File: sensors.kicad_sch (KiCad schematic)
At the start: 25 parts, among them J11 GND, J14 3.3v, J15 SDA, J16 SCL, U10 BHI360, U21 PCA9517DP,118, U33 BME688_C3664478, U34 BMI270

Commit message: Remove Badge.Team branding
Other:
- company: Badge.Team -> Nicolai Electronics
- title: WHY2025 badge -> Tanmatsu
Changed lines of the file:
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@@
 	(paper "A4")
 	(title_block
-		(title "WHY2025 badge")
-		(date "2024-11-01")
-		(rev "Prototype 3")
-		(company "Badge.Team")
-		(comment 1 "Copyright 2024 Nicolai Electronics")
-		(comment 2 "License: CERN-OHL-P")
-		(comment 3 "Untested prototype design")
+		(title "Tanmatsu")
+		(date "2024-11-20")
+		(rev "Prototype 4")
+		(company "Nicolai Electronics")
+		(comment 1 "Copyright 2024 Paul Honig")
+		(comment 2 "Copyright 2024 Nicolai Electronics")
+		(comment 3 "License: CERN-OHL-P")
 	)
 	(junction

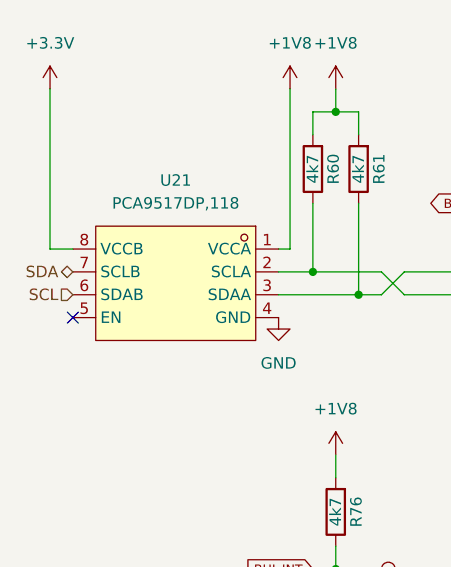
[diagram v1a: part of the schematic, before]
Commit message: Fix SDA/SCL swap.
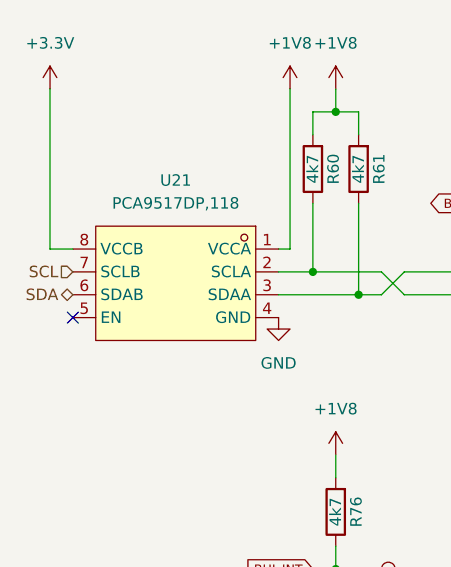
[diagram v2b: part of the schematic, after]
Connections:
- net SCL: now also U21.7 (SCLB); no longer U21.6 (SDAB)
- net SDA: now also U21.6 (SDAB); no longer U21.7 (SCLB)
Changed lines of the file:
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@@
 	(hierarchical_label "SCL"
 		(shape input)
-		(at 33.02 63.5 180)
+		(at 33.02 60.96 180)
 		(fields_autoplaced yes)
 		(effects
@@
 	(hierarchical_label "SDA"
 		(shape bidirectional)
-		(at 33.02 60.96 180)
+		(at 33.02 63.5 180)
 		(fields_autoplaced yes)
 		(effects

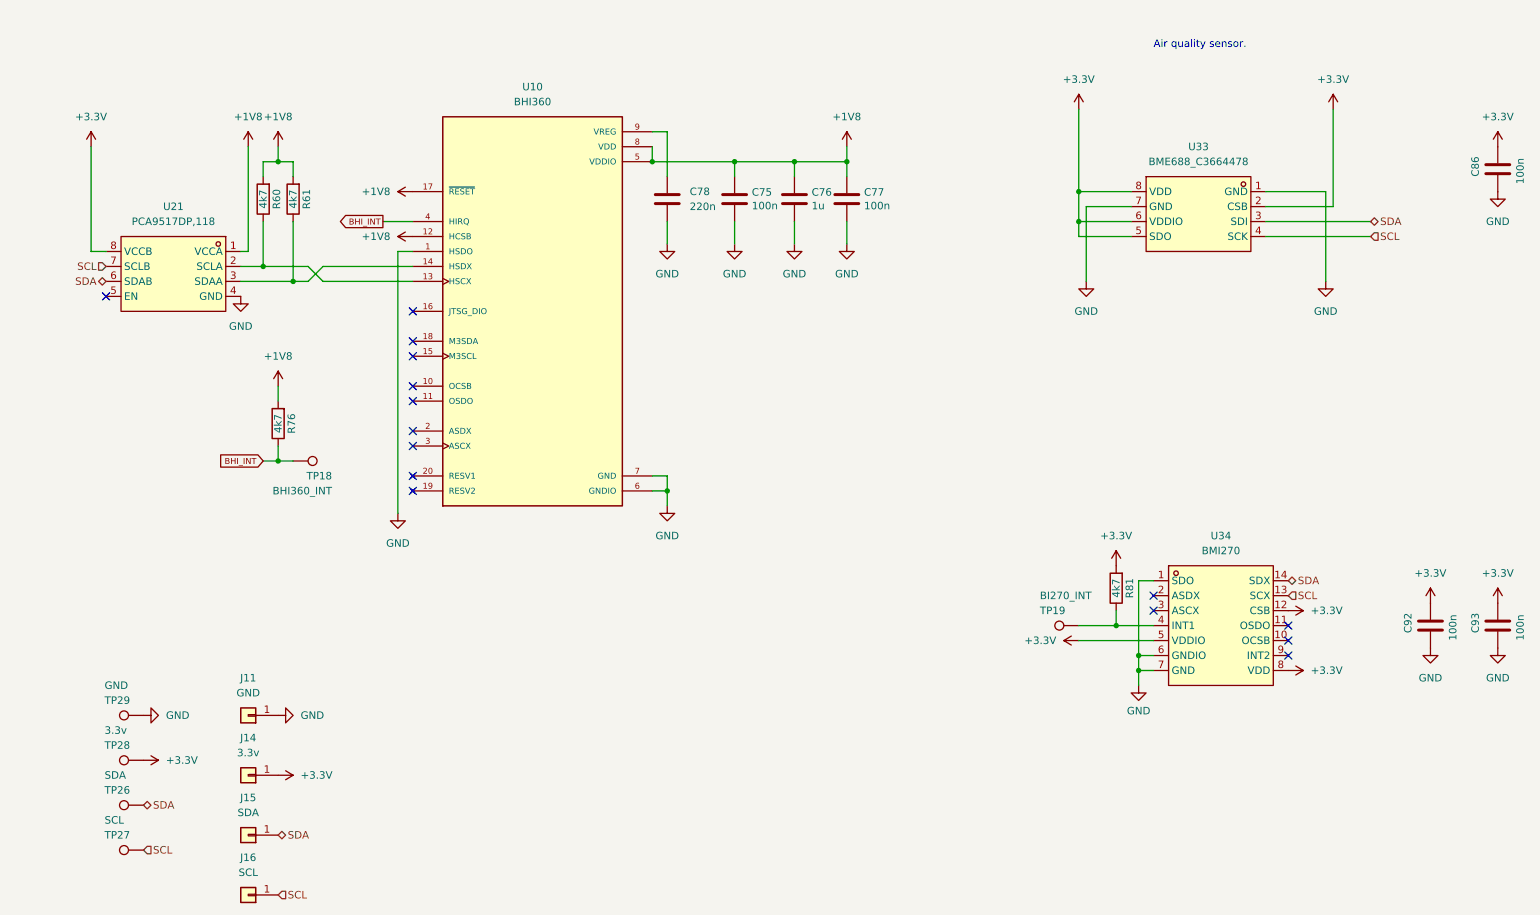
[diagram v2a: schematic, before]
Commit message: Remove Bosch sensors, add header for CO2 sensor
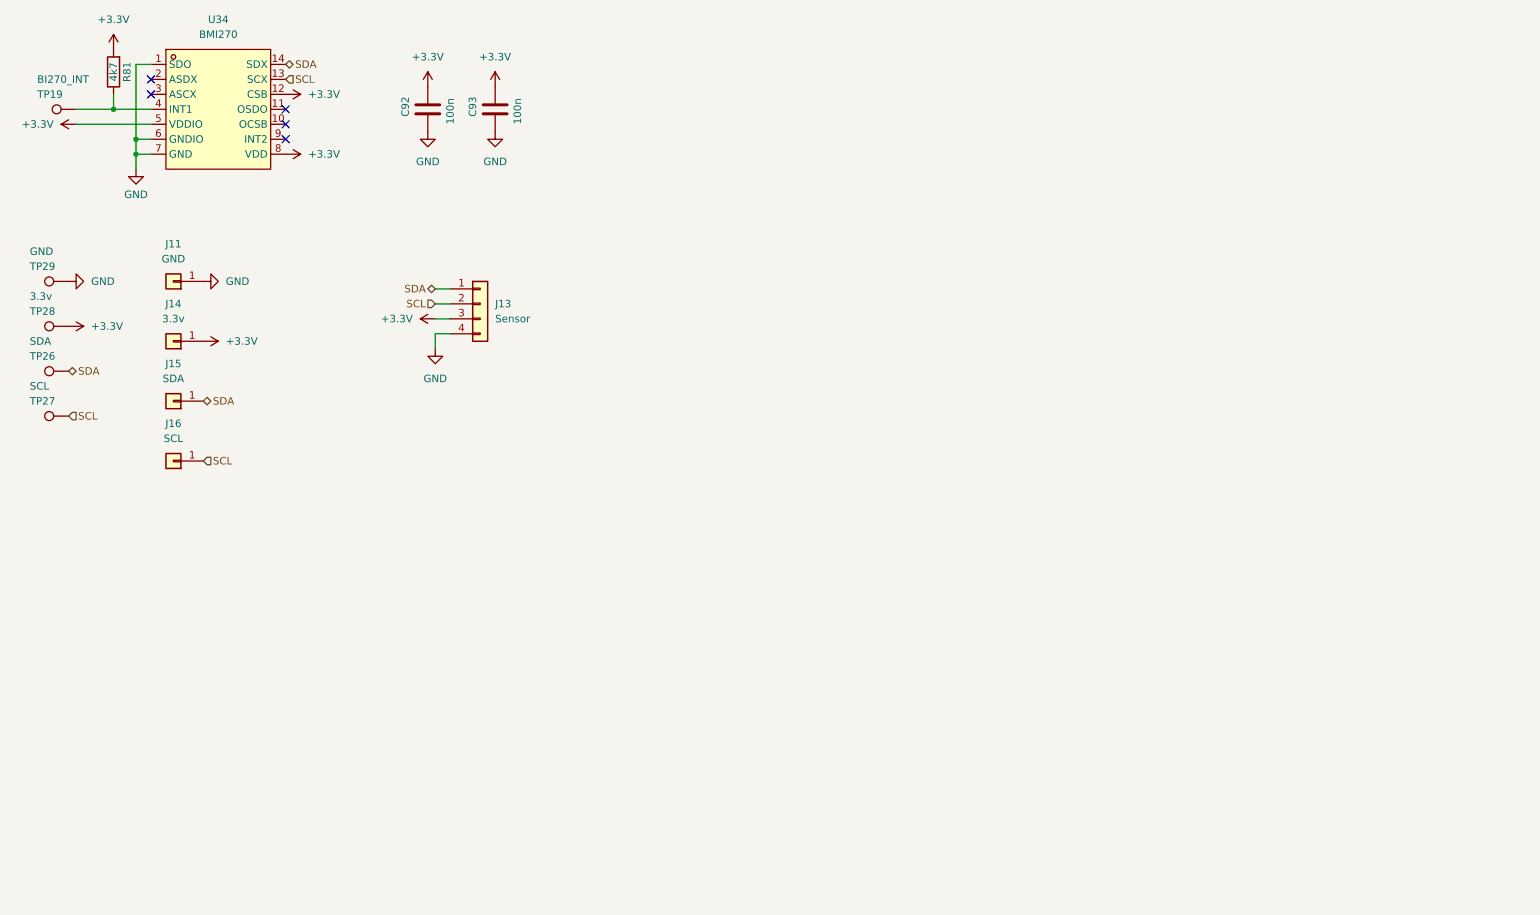
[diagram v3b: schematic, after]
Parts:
- removed C75, C77: 100n, Capacitor_SMD:C_0402_1005Metric, symbol symbols:C
- removed C76: 1u, Capacitor_SMD:C_0603_1608Metric, symbol symbols:C
- removed C78: 220n, Capacitor_SMD:C_0603_1608Metric, symbol Device:C
- removed C86: 100n, Capacitor_SMD:C_0402_1005Metric, symbol mch2021-rescue:C-Device
- removed R60, R61, R76: 4k7, Resistor_SMD:R_0402_1005Metric, symbol Device:R
- removed TP18: BHI360_INT, TestPoint:TestPoint_Pad_D1.0mm, symbol Connector:TestPoint
- removed U10: BHI360, library:XDCR_BHI360, symbol BHI360:BHI360
- removed U21: PCA9517DP,118, library:TSSOP-8_L3.0-W3.0-P0.65-LS4.9-BL, symbol lcsc:PCA9517DP,118
- removed U33: BME688_C3664478, lcsc:LGA-8_L3.0-W3.0-P0.80_BME688, symbol lcsc:BME688_C3664478
- added J13: Sensor, Connector_PinHeader_2.54mm:PinHeader_1x04_P2.54mm_Vertical, symbol Connector_Generic:Conn_01x04
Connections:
- net +3.3V: now also J13.3 (Pin_3)
- net GND: now also J13.4 (Pin_4)
- net SCL: now also J13.2 (Pin_2)
- net SDA: now also J13.1 (Pin_1)
- no-connect marks 15 -> 5
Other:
- note removed: "Air quality sensor."
- moved on the sheet: C92, C93, J11, J14, J15, J16, R81, TP19, TP26, TP27, TP28, TP29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

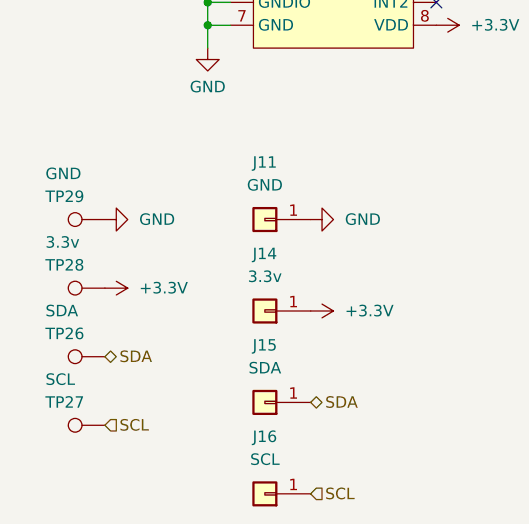
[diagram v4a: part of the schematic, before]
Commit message: Add MCH2022 style battery connector as DNP, use correct footprint for PH style battery connector
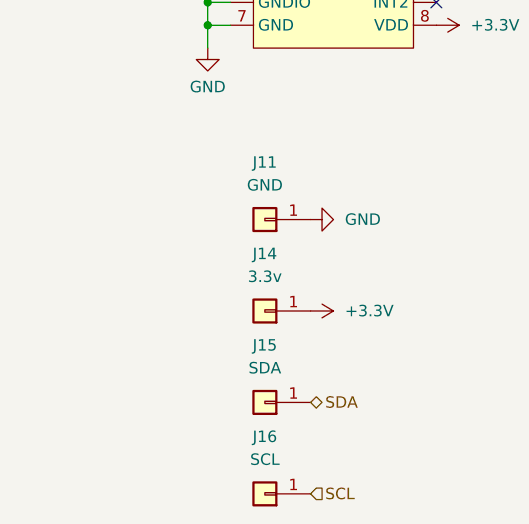
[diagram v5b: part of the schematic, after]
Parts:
- removed TP26: SDA, TestPoint:TestPoint_Pad_D1.0mm, symbol Connector:TestPoint
- removed TP27: SCL, TestPoint:TestPoint_Pad_D1.0mm, symbol Connector:TestPoint
- removed TP28: 3.3v, TestPoint:TestPoint_Pad_D1.0mm, symbol Connector:TestPoint
- removed TP29: GND, TestPoint:TestPoint_Pad_D1.0mm, symbol Connector:TestPoint

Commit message: Tanmatsu prototype
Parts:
- renumbered C92 to C83, C93 to C84, J11 to J15, J13 to J16, J14 to J17, J15 to J18, J16 to J19, R81 to R82, TP19 to TP22, U34 to U30
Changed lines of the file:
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@@
 	(title_block
 		(title "Tanmatsu")
-		(date "2024-12-24")
-		(rev "Prototype")
+		(date "2024-12-30")
+		(rev "0.9")
 		(company "Nicolai Electronics")
 		(comment 1 "Copyright 2024 Paul Honig")
@@
 		(dnp no)
 		(fields_autoplaced yes)
-		(property "Reference" "#PWR0310"
+		(property "Reference" "#PWR0293"
 			(at 45.72 73.66 0)
 			(effects
@@
 			(project "why2025"
 				(path "/6a31734e-65de-48f3-8156-2b24b665b183/14d9c0ee-00ab-4a1b-b059-e8045c71d6ae"
-					(reference "#PWR0310")
+					(reference "#PWR0293")
 					(unit 1)
 				)
@@
 		(on_board yes)
 		(dnp no)
-		(property "Reference" "#PWR0306"
+		(property "Reference" "#PWR0287"
 			(at 87.63 44.45 0)
 			(effects
@@
 			(project "why2025"
 				(path "/6a31734e-65de-48f3-8156-2b24b665b183/14d9c0ee-00ab-4a1b-b059-e8045c71d6ae"
-					(reference "#PWR0306")
+					(reference "#PWR0287")
 					(unit 1)
 				)
@@
 		(dnp no)
 		(fields_autoplaced yes)
-		(property "Reference" "J14"
+		(property "Reference" "J17"
 			(at 44.45 67.31 0)
 			(effects
@@
 			(project "why2025"
 				(path "/6a31734e-65de-48f3-8156-2b24b665b183/14d9c0ee-00ab-4a1b-b059-e8045c71d6ae"
-					(reference "J14")
+					(reference "J17")
 					(unit 1)
 				)
@@
 		(dnp no)
 		(fields_autoplaced yes)
-		(property "Reference" "#PWR0288"
+		(property "Reference" "#PWR0289"
 			(at 59.69 41.91 0)
 			(effects
@@
 			(project "why2025"
 				(path "/6a31734e-65de-48f3-8156-2b24b665b183/14d9c0ee-00ab-4a1b-b059-e8045c71d6ae"
-					(reference "#PWR0288")
+					(reference "#PWR0289")
 					(unit 1)
 				)
@@
 		(dnp no)
 		(fields_autoplaced yes)
-		(property "Reference" "#PWR0304"
+		(property "Reference" "#PWR0285"
 			(at 59.69 31.75 0)
 			(effects
@@
 			(project "why2025"
 				(path "/6a31734e-65de-48f3-8156-2b24b665b183/14d9c0ee-00ab-4a1b-b059-e8045c71d6ae"
-					(reference "#PWR0304")
+					(reference "#PWR0285")
 					(unit 1)
 				)
@@
 		(on_board yes)
 		(dnp no)
-		(property "Reference" "TP19"
+		(property "Reference" "TP22"
 			(at 21.336 31.75 90)
 			(effects
@@
 			(project "why2025"
 				(path "/6a31734e-65de-48f3-8156-2b24b665b183/14d9c0ee-00ab-4a1b-b059-e8045c71d6ae"
-					(reference "TP19")
+					(reference "TP22")
 					(unit 1)
 				)
@@
 		(dnp no)
 		(fields_autoplaced yes)
-		(property "Reference" "J11"
+		(property "Reference" "J15"
 			(at 44.45 57.15 0)
 			(effects
@@
 			(project "why2025"
 				(path "/6a31734e-65de-48f3-8156-2b24b665b183/14d9c0ee-00ab-4a1b-b059-e8045c71d6ae"
-					(reference "J11")
+					(reference "J15")
 					(unit 1)
 				)
@@
 		(dnp no)
 		(fields_autoplaced yes)
-		(property "Reference" "#PWR0309"
+		(property "Reference" "#PWR0291"
 			(at 55.88 63.5 0)
 			(effects
@@
 			(project "why2025"
 				(path "/6a31734e-65de-48f3-8156-2b24b665b183/14d9c0ee-00ab-4a1b-b059-e8045c71d6ae"
-					(reference "#PWR0309")
+					(reference "#PWR0291")
 					(unit 1)
 				)
@@
 		(on_board yes)
 		(dnp no)
-		(property "Reference" "C92"
+		(property "Reference" "C83"
 			(at 83.82 35.56 90)
 			(effects
@@
 			(project "why2025"
 				(path "/6a31734e-65de-48f3-8156-2b24b665b183/14d9c0ee-00ab-4a1b-b059-e8045c71d6ae"
-					(reference "C92")
+					(reference "C83")
 					(unit 1)
 				)
@@
 		(dnp no)
 		(fields_autoplaced yes)
-		(property "Reference" "#PWR0305"
+		(property "Reference" "#PWR0283"
 			(at 87.63 34.29 0)
 			(effects
@@
 			(project "why2025"
 				(path "/6a31734e-65de-48f3-8156-2b24b665b183/14d9c0ee-00ab-4a1b-b059-e8045c71d6ae"
-					(reference "#PWR0305")
+					(reference "#PWR0283")
 					(unit 1)
 				)
@@
 		(dnp no)
 		(fields_autoplaced yes)
-		(property "Reference" "J13"
+		(property "Reference" "J16"
 			(at 99.06 67.3099 0)
 			(effects
@@
 			(project ""
 				(path "/6a31734e-65de-48f3-8156-2b24b665b183/14d9c0ee-00ab-4a1b-b059-e8045c71d6ae"
-					(reference "J13")
+					(reference "J16")
 					(unit 1)
 				)
@@
 		(dnp no)
 		(fields_autoplaced yes)
-		(property "Reference" "#PWR0307"
+		(property "Reference" "#PWR0284"
 			(at 99.06 34.29 0)
 			(effects
@@
 			(project "why2025"
 				(path "/6a31734e-65de-48f3-8156-2b24b665b183/14d9c0ee-00ab-4a1b-b059-e8045c71d6ae"
-					(reference "#PWR0307")
+					(reference "#PWR0284")
 					(unit 1)
 				)
@@
 		(dnp no)
 		(fields_autoplaced yes)
-		(property "Reference" "#PWR0115"
+		(property "Reference" "#PWR0292"
 			(at 92.71 69.85 0)
 			(effects
@@
 			(project "tanmatsu"
 				(path "/6a31734e-65de-48f3-8156-2b24b665b183/14d9c0ee-00ab-4a1b-b059-e8045c71d6ae"
-					(reference "#PWR0115")
+					(reference "#PWR0292")
 					(unit 1)
 				)
@@
 		(on_board yes)
 		(dnp no)
-		(property "Reference" "#PWR0279"
+		(property "Reference" "#PWR0290"
 			(at 38.1 50.8 0)
 			(effects
@@
 			(project "why2025"
 				(path "/6a31734e-65de-48f3-8156-2b24b665b183/14d9c0ee-00ab-4a1b-b059-e8045c71d6ae"
-					(reference "#PWR0279")
+					(reference "#PWR0290")
 					(unit 1)
 				)
@@
 		(dnp no)
 		(fields_autoplaced yes)
-		(property "Reference" "J16"
+		(property "Reference" "J19"
 			(at 44.45 87.63 0)
 			(effects
@@
 			(project "why2025"
 				(path "/6a31734e-65de-48f3-8156-2b24b665b183/14d9c0ee-00ab-4a1b-b059-e8045c71d6ae"
-					(reference "J16")
+					(reference "J19")
 					(unit 1)
 				)
@@
 		(dnp no)
 		(fields_autoplaced yes)
-		(property "Reference" "#PWR0280"
+		(property "Reference" "#PWR0286"
 			(at 31.75 36.83 0)
 			(effects
@@
 			(project "why2025"
 				(path "/6a31734e-65de-48f3-8156-2b24b665b183/14d9c0ee-00ab-4a1b-b059-e8045c71d6ae"
-					(reference "#PWR0280")
+					(reference "#PWR0286")
 					(unit 1)
 				)
@@
 		(dnp no)
 		(fields_autoplaced yes)
-		(property "Reference" "#PWR071"
+		(property "Reference" "#PWR0294"
 			(at 88.9 81.28 0)
 			(effects
@@
 			(project "tanmatsu"
 				(path "/6a31734e-65de-48f3-8156-2b24b665b183/14d9c0ee-00ab-4a1b-b059-e8045c71d6ae"
-					(reference "#PWR071")
+					(reference "#PWR0294")
 					(unit 1)
 				)
@@
 		(on_board yes)
 		(dnp no)
-		(property "Reference" "#PWR0308"
+		(property "Reference" "#PWR0288"
 			(at 99.06 44.45 0)
 			(effects
@@
 			(project "why2025"
 				(path "/6a31734e-65de-48f3-8156-2b24b665b183/14d9c0ee-00ab-4a1b-b059-e8045c71d6ae"
-					(reference "#PWR0308")
+					(reference "#PWR0288")
 					(unit 1)
 				)
@@
 		(on_board yes)
 		(dnp no)
-		(property "Reference" "R81"
+		(property "Reference" "R82"
 			(at 36.576 27.94 90)
 			(effects
@@
 			(project "why2025"
 				(path "/6a31734e-65de-48f3-8156-2b24b665b183/14d9c0ee-00ab-4a1b-b059-e8045c71d6ae"
-					(reference "R81")
+					(reference "R82")
 					(unit 1)
 				)
@@
 		(dnp no)
 		(fields_autoplaced yes)
-		(property "Reference" "J15"
+		(property "Reference" "J18"
 			(at 44.45 77.47 0)
 			(effects
@@
 			(project "why2025"
 				(path "/6a31734e-65de-48f3-8156-2b24b665b183/14d9c0ee-00ab-4a1b-b059-e8045c71d6ae"
-					(reference "J15")
+					(reference "J18")
 					(unit 1)
 				)
@@
 		(dnp no)
 		(fields_autoplaced yes)
-		(property "Reference" "#PWR0273"
+		(property "Reference" "#PWR0282"
 			(at 34.29 27.94 0)
 			(effects
@@
 			(project "why2025"
 				(path "/6a31734e-65de-48f3-8156-2b24b665b183/14d9c0ee-00ab-4a1b-b059-e8045c71d6ae"
-					(reference "#PWR0273")
+					(reference "#PWR0282")
 					(unit 1)
 				)
@@
 		(dnp no)
 		(fields_autoplaced yes)
-		(property "Reference" "U34"
+		(property "Reference" "U30"
 			(at 52.07 19.05 0)
 			(effects
@@
 			(project ""
 				(path "/6a31734e-65de-48f3-8156-2b24b665b183/14d9c0ee-00ab-4a1b-b059-e8045c71d6ae"
-					(reference "U34")
+					(reference "U30")
 					(unit 1)
 				)
@@
 		(on_board yes)
 		(dnp no)
-		(property "Reference" "C93"
+		(property "Reference" "C84"
 			(at 95.25 35.56 90)
 			(effects
@@
 			(project "why2025"
 				(path "/6a31734e-65de-48f3-8156-2b24b665b183/14d9c0ee-00ab-4a1b-b059-e8045c71d6ae"
-					(reference "C93")
-					(unit 1)
-				)
+					(reference "C84")
+					(unit 1)
+				)
